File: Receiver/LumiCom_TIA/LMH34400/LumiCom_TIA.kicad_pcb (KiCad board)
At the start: 4 copper layers, 90 x 40 mm, 52 parts, among them J1 TEST, J10 OUT, J2 Conn_Coaxial, J3 Vout, J4 N_EN, J5 N_ALC, J6 Conn_Coaxial, J7 IN, J8 Vout, J9 TEST, U1 XLMH34400IDRLR, U2 LTC6268-10-SOT23

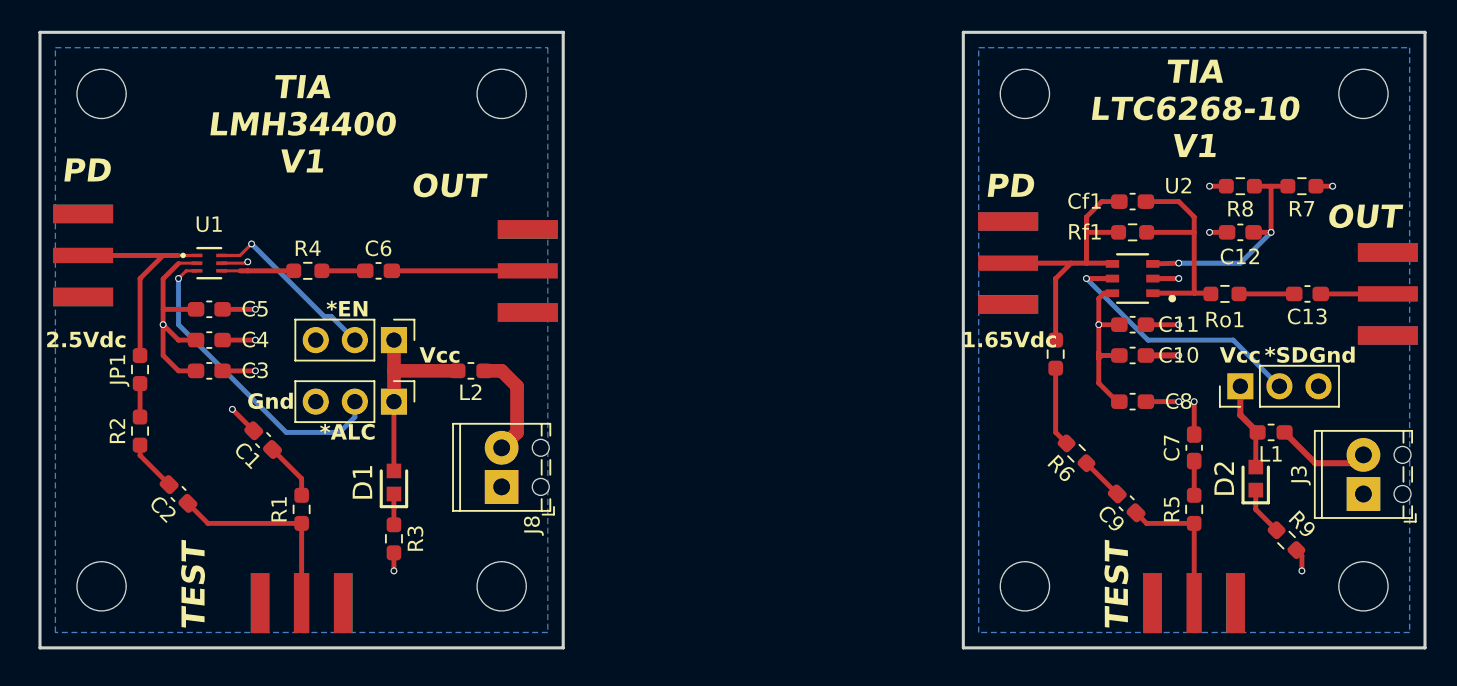
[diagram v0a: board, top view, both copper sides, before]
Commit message: Multiple updates
SMA, Screw terminals, track widths, added some optional 0 ohm bypass resistors
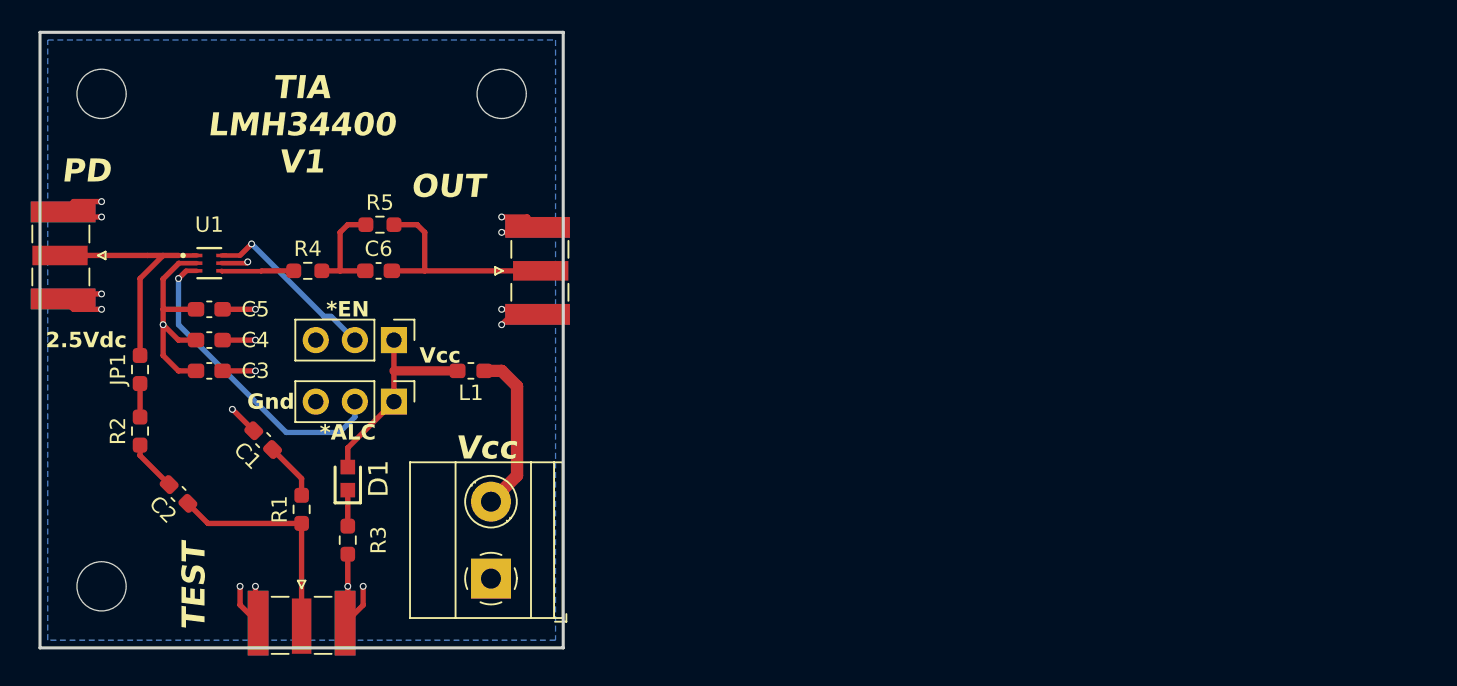
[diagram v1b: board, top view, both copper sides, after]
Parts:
- removed C10, C13, C7, C9: 1uF, Capacitor_SMD:C_0603_1608Metric_Pad1.08x0.95mm_HandSolder
- removed C11: 100nF, Capacitor_SMD:C_0603_1608Metric_Pad1.08x0.95mm_HandSolder
- removed C12, C8, Cf1: 10uF, Capacitor_SMD:C_0603_1608Metric_Pad1.08x0.95mm_HandSolder
- removed D2: 150060VS75000, LumiCom_TIA:LEDC1608X80N
- removed H4, H5, H6, H7, H8: M3, MountingHole:MountingHole_3.2mm_M3_DIN965
- removed J10: OUT, LumiCom_TIA:RFSOLUTIONS_CON-SMA-EDGE-S
- removed J7: IN, LumiCom_TIA:RFSOLUTIONS_CON-SMA-EDGE-S
- removed J8: Vout, TerminalBlock_Phoenix:TerminalBlock_Phoenix_MPT-0,5-2-2.54_1x02_P2.54mm_Horizontal
- removed J9: TEST, LumiCom_TIA:RFSOLUTIONS_CON-SMA-EDGE-S
- removed JP2: Test, Resistor_SMD:R_0603_1608Metric_Pad0.98x0.95mm_HandSolder
- removed L2: BLM18BA100SN1D, Inductor_SMD:L_0603_1608Metric_Pad1.05x0.95mm_HandSolder
- removed R6: 4.02K, Resistor_SMD:R_0603_1608Metric_Pad0.98x0.95mm_HandSolder
- removed R7, R8: 20k, Resistor_SMD:R_0603_1608Metric_Pad0.98x0.95mm_HandSolder
- removed R9: 1k2, Resistor_SMD:R_0603_1608Metric_Pad0.98x0.95mm_HandSolder
- removed Rf1: 10K, Resistor_SMD:R_0603_1608Metric_Pad0.98x0.95mm_HandSolder
- removed Ro1: 50, Resistor_SMD:R_0603_1608Metric_Pad0.98x0.95mm_HandSolder
- removed SD_L1: SD_L, Connector_PinHeader_2.54mm:PinHeader_1x03_P2.54mm_Vertical
- removed U2: LTC6268-10-SOT23, LumiCom_TIA:TSOT-23_S6_LIT
- J1, J2, J6: footprint LumiCom_TIA:RFSOLUTIONS_CON-SMA-EDGE-S -> Connector_Coaxial:SMA_Samtec_SMA-J-P-X-ST-EM1_EdgeMount
- J3: footprint TerminalBlock_Phoenix:TerminalBlock_Phoenix_MPT-0,5-2-2.54_1x02_P2.54mm_Horizontal -> TerminalBlock_Phoenix:TerminalBlock_Phoenix_MKDS-1,5-2_1x02_P5.00mm_Horizontal
- R5: value 50 -> 0
- moved J3 57.0 mm to (136.3, 88.5)
- moved R5 56.1 mm to (129.1, 65.5), turned to 0 degrees
- moved L1 52.2 mm to (135.0, 75.0)
- moved D1 3.01 mm to (127.0, 82.0)
- moved R3 3.00 mm to (127.0, 86.0)
- moved J6 0.66 mm to (139.3, 68.5), turned to 90 degrees
- turned J1 to 0 degrees
- turned J2 to -90 degrees
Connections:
- R5 pad 1: Net-(J9-In) -> Net-(C6-Pad1)
- R5 pad 2: Net-(C7-Pad1) -> Net-(J6-In)
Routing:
- net Net-(J7-In): track 19.8 -> 0.00 mm
- net GND: track 25.2 -> 43.9 mm, vias 14 -> 17
- net VCC: track 45.8 -> 28.5 mm, vias 3 -> 1
- net /ltc6269-10/Shutdown_L: track 17.1 -> 0.00 mm, vias 1 -> 0
- net Net-(U2-OUT): track 15.4 -> 0.00 mm
- net Net-(U2-+IN): track 14.8 -> 0.00 mm, vias 2 -> 0
- net Net-(J9-In): track 9.24 -> 0.00 mm
- net Net-(J8-Pin_2): track 6.95 -> 0.00 mm
- net Net-(JP2-A): track 5.18 -> 0.00 mm
- net Net-(J3-Pin_2): track 6.18 -> 10.7 mm
- net Net-(C6-Pad1): track 2.82 -> 7.21 mm
- net Net-(J10-In): track 4.37 -> 0.00 mm
- net Net-(J6-In): track 9.73 -> 13.9 mm
- net Net-(C13-Pad1): track 3.59 -> 0.00 mm
- net Net-(D2-K): track 3.17 -> 0.00 mm
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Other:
- board size 90 x 40 mm -> 34 x 40 mm
- board text added: "Board thickness: 1.2mm 4 Layers"
- board text removed: "*SD"
- board text removed: "1.65Vdc"
- board text removed: "TIA LTC6268-10 V1"
